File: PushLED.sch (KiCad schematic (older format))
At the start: 3 parts, among them Q1 BC847, SW3 SW_Push_LED

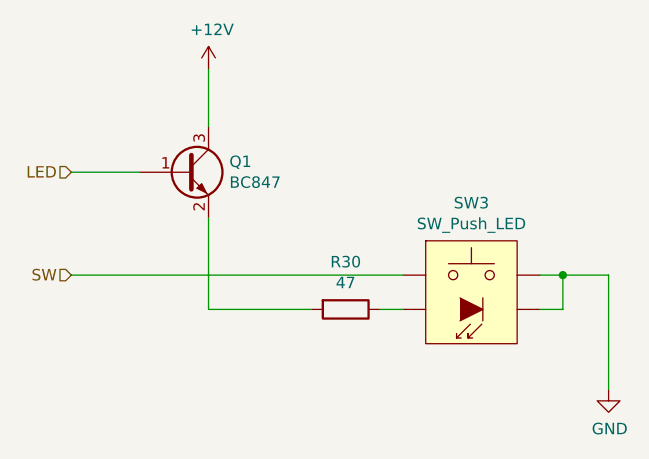
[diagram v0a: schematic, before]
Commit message: Moved codec to audio module.
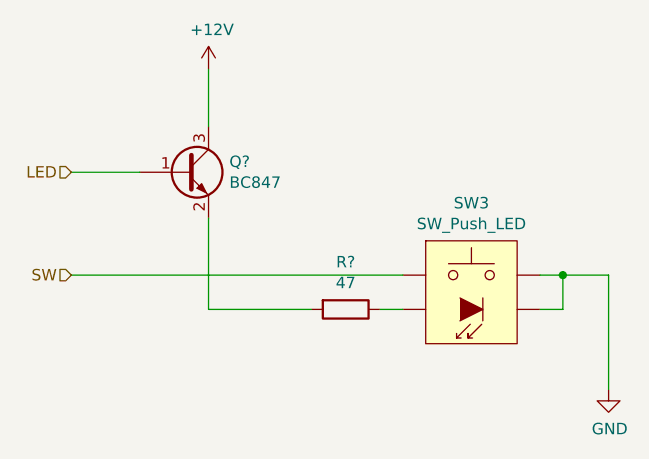
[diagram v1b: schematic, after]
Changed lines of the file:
@@
 AR Path="/61DB1EC2/5DB13571/5DA98203" Ref="#PWR?"  Part="1"
 AR Path="/61DC9CE4/5DA98203" Ref="#PWR055"  Part="1"
-F 0 "#PWR055" H 6250 4000 50  0001 C CNN
+AR Path="/6220B257/5DA98203" Ref="#PWR?"  Part="1"
+AR Path="/62210337/5DA98203" Ref="#PWR?"  Part="1"
+AR Path="/62210785/5DA98203" Ref="#PWR?"  Part="1"
+F 0 "#PWR?" H 6250 4000 50  0001 C CNN
 F 1 "GND" H 6255 4077 50  0000 C CNN
 F 2 "" H 6250 4250 50  0001 C CNN
@@
 AR Path="/61DB1EC2/5DB13571/5DA98210" Ref="R?"  Part="1"
 AR Path="/61DC9CE4/5DA98210" Ref="R30"  Part="1"
-F 0 "R30" V 4893 3900 50  0000 C CNN
+AR Path="/6220B257/5DA98210" Ref="R?"  Part="1"
+AR Path="/62210337/5DA98210" Ref="R?"  Part="1"
+AR Path="/62210785/5DA98210" Ref="R?"  Part="1"
+F 0 "R?" V 4893 3900 50  0000 C CNN
 F 1 "47" V 4984 3900 50  0000 C CNN
 F 2 "Resistor_SMD:R_0603_1608Metric" V 5030 3900 50  0001 C CNN
@@
 AR Path="/61DB1EC2/5DB13571/5DA9821D" Ref="Q?"  Part="1"
 AR Path="/61DC9CE4/5DA9821D" Ref="Q1"  Part="1"
-F 0 "Q1" H 4591 3346 50  0000 L CNN
+AR Path="/6220B257/5DA9821D" Ref="Q?"  Part="1"
+AR Path="/62210337/5DA9821D" Ref="Q?"  Part="1"
+AR Path="/62210785/5DA9821D" Ref="Q?"  Part="1"
+F 0 "Q?" H 4591 3346 50  0000 L CNN
 F 1 "BC847" H 4591 3255 50  0000 L CNN
 F 2 "Package_TO_SOT_SMD:SOT-23" H 4600 3225 50  0001 L CIN
@@
 AR Path="/61DB1EC2/5DB13571/5DA99988" Ref="#PWR?"  Part="1"
 AR Path="/61DC9CE4/5DA99988" Ref="#PWR054"  Part="1"
-F 0 "#PWR054" H 4500 2700 50  0001 C CNN
+AR Path="/6220B257/5DA99988" Ref="#PWR?"  Part="1"
+AR Path="/62210337/5DA99988" Ref="#PWR?"  Part="1"
+AR Path="/62210785/5DA99988" Ref="#PWR?"  Part="1"
+F 0 "#PWR?" H 4500 2700 50  0001 C CNN
 F 1 "+12V" H 4515 3023 50  0000 C CNN
 F 2 "" H 4500 2850 50  0001 C CNN
@@
 U 1 1 61E253E8
 P 5650 3750
-F 0 "SW3" H 5650 4065 50  0000 C CNN
+AR Path="/61DC9CE4/61E253E8" Ref="SW3"  Part="1"
+AR Path="/6220B257/61E253E8" Ref="SW?"  Part="1"
+AR Path="/62210337/61E253E8" Ref="SW?"  Part="1"
+AR Path="/62210785/61E253E8" Ref="SW?"  Part="1"
+F 0 "SW?" H 5650 4065 50  0000 C CNN
 F 1 "SW_Push_LED" H 5650 3974 50  0000 C CNN
 F 2 "" H 5650 3950 50  0001 C CNN

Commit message: Re-annotation.
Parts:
- added C26: 100n, symbol Device:C
- added R10: 10k, symbol Device:R
- renumbered R30 to R9
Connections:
- net GND: now also C26.2
- net SW: now also C26.1, R10.2
- new net +3V3: R10.1
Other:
- moved on the sheet: Q6
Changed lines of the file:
@@
 $Descr A4 11693 8268
 encoding utf-8
-Sheet 4 6
+Sheet 3 11
 Title ""
 Date ""
@@
 AR Path="/61DB1EC2/5E023019/5DA98203" Ref="#PWR?"  Part="1"
 AR Path="/61DB1EC2/5DB13571/5DA98203" Ref="#PWR?"  Part="1"
-AR Path="/61DC9CE4/5DA98203" Ref="#PWR055"  Part="1"
-AR Path="/6220B257/5DA98203" Ref="#PWR?"  Part="1"
-AR Path="/62210337/5DA98203" Ref="#PWR?"  Part="1"
-AR Path="/62210785/5DA98203" Ref="#PWR?"  Part="1"
-F 0 "#PWR?" H 6250 4000 50  0001 C CNN
+AR Path="/61DC9CE4/5DA98203" Ref="#PWR035"  Part="1"
+AR Path="/6220B257/5DA98203" Ref="#PWR092"  Part="1"
+AR Path="/62210337/5DA98203" Ref="#PWR096"  Part="1"
+AR Path="/62210785/5DA98203" Ref="#PWR0100"  Part="1"
+F 0 "#PWR0100" H 6250 4000 50  0001 C CNN
 F 1 "GND" H 6255 4077 50  0000 C CNN
 F 2 "" H 6250 4250 50  0001 C CNN
@@
 AR Path="/61DB1EC2/5E023019/5DA98210" Ref="R?"  Part="1"
 AR Path="/61DB1EC2/5DB13571/5DA98210" Ref="R?"  Part="1"
-AR Path="/61DC9CE4/5DA98210" Ref="R30"  Part="1"
-AR Path="/6220B257/5DA98210" Ref="R?"  Part="1"
-AR Path="/62210337/5DA98210" Ref="R?"  Part="1"
-AR Path="/62210785/5DA98210" Ref="R?"  Part="1"
-F 0 "R?" V 4893 3900 50  0000 C CNN
+AR Path="/61DC9CE4/5DA98210" Ref="R9"  Part="1"
+AR Path="/6220B257/5DA98210" Ref="R60"  Part="1"
+AR Path="/62210337/5DA98210" Ref="R62"  Part="1"
+AR Path="/62210785/5DA98210" Ref="R64"  Part="1"
+F 0 "R64" V 4893 3900 50  0000 C CNN
 F 1 "47" V 4984 3900 50  0000 C CNN
 F 2 "Resistor_SMD:R_0603_1608Metric" V 5030 3900 50  0001 C CNN
@@
 L Transistor_BJT:BC847 Q?
 U 1 1 5DA9821D
-P 4400 3300
+P 4550 3300
 AR Path="/5C756F9B/5DA9821D" Ref="Q?"  Part="1"
 AR Path="/5C763CB7/5DA9821D" Ref="Q?"  Part="1"
@@
 AR Path="/61DB1EC2/5DB13571/5DA9821D" Ref="Q?"  Part="1"
 AR Path="/61DC9CE4/5DA9821D" Ref="Q1"  Part="1"
-AR Path="/6220B257/5DA9821D" Ref="Q?"  Part="1"
-AR Path="/62210337/5DA9821D" Ref="Q?"  Part="1"
-AR Path="/62210785/5DA9821D" Ref="Q?"  Part="1"
-F 0 "Q?" H 4591 3346 50  0000 L CNN
-F 1 "BC847" H 4591 3255 50  0000 L CNN
-F 2 "Package_TO_SOT_SMD:SOT-23" H 4600 3225 50  0001 L CIN
-F 3 "http://www.infineon.com/dgdl/Infineon-BC847SERIES_BC848SERIES_BC849SERIES_BC850SERIES-DS-v01_01-en.pdf?fileId=db3a304314dca389011541d4630a1657" H 4400 3300 50  0001 L CNN
-	1    4400 3300
-	1    0    0    -1
-$EndComp
-Wire Wire Line
-	4500 3500 4500 3900
-Wire Wire Line
-	4500 3900 4950 3900
+AR Path="/6220B257/5DA9821D" Ref="Q4"  Part="1"
+AR Path="/62210337/5DA9821D" Ref="Q5"  Part="1"
+AR Path="/62210785/5DA9821D" Ref="Q6"  Part="1"
+F 0 "Q6" H 4741 3346 50  0000 L CNN
+F 1 "BC847" H 4741 3255 50  0000 L CNN
+F 2 "Package_TO_SOT_SMD:SOT-23" H 4750 3225 50  0001 L CIN
+F 3 "http://www.infineon.com/dgdl/Infineon-BC847SERIES_BC848SERIES_BC849SERIES_BC850SERIES-DS-v01_01-en.pdf?fileId=db3a304314dca389011541d4630a1657" H 4550 3300 50  0001 L CNN
+	1    4550 3300
+	1    0    0    -1
+$EndComp
+Wire Wire Line
+	4650 3500 4650 3900
 Text HLabel 3900 3300 0    50   Input ~ 0
 LED
-Wire Wire Line
-	3900 3300 4200 3300
 Text HLabel 3900 3750 0    50   Input ~ 0
 SW
-Wire Wire Line
-	3900 3750 5350 3750
 $Comp
 L power:+12V #PWR?
 U 1 1 5DA99988
-P 4500 2850
+P 4650 2850
 AR Path="/5DA90748/5DA99988" Ref="#PWR?"  Part="1"
 AR Path="/5DAF110B/5DA99988" Ref="#PWR?"  Part="1"
@@
 AR Path="/61DB1EC2/5E023019/5DA99988" Ref="#PWR?"  Part="1"
 AR Path="/61DB1EC2/5DB13571/5DA99988" Ref="#PWR?"  Part="1"
-AR Path="/61DC9CE4/5DA99988" Ref="#PWR054"  Part="1"
-AR Path="/6220B257/5DA99988" Ref="#PWR?"  Part="1"
-AR Path="/62210337/5DA99988" Ref="#PWR?"  Part="1"
-AR Path="/62210785/5DA99988" Ref="#PWR?"  Part="1"
-F 0 "#PWR?" H 4500 2700 50  0001 C CNN
-F 1 "+12V" H 4515 3023 50  0000 C CNN
-F 2 "" H 4500 2850 50  0001 C CNN
-F 3 "" H 4500 2850 50  0001 C CNN
-	1    4500 2850
-	1    0    0    -1
-$EndComp
-Wire Wire Line
-	4500 2850 4500 3100
+AR Path="/61DC9CE4/5DA99988" Ref="#PWR033"  Part="1"
+AR Path="/6220B257/5DA99988" Ref="#PWR090"  Part="1"
+AR Path="/62210337/5DA99988" Ref="#PWR094"  Part="1"
+AR Path="/62210785/5DA99988" Ref="#PWR098"  Part="1"
+F 0 "#PWR098" H 4650 2700 50  0001 C CNN
+F 1 "+12V" H 4665 3023 50  0000 C CNN
+F 2 "" H 4650 2850 50  0001 C CNN
+F 3 "" H 4650 2850 50  0001 C CNN
+	1    4650 2850
+	1    0    0    -1
+$EndComp
+Wire Wire Line
+	4650 2850 4650 3100
 $Comp
 L SW_PUSH_LED:SW_Push_LED SW3
@@
 P 5650 3750
 AR Path="/61DC9CE4/61E253E8" Ref="SW3"  Part="1"
-AR Path="/6220B257/61E253E8" Ref="SW?"  Part="1"
-AR Path="/62210337/61E253E8" Ref="SW?"  Part="1"
-AR Path="/62210785/61E253E8" Ref="SW?"  Part="1"
-F 0 "SW?" H 5650 4065 50  0000 C CNN
+AR Path="/6220B257/61E253E8" Ref="SW4"  Part="1"
+AR Path="/62210337/61E253E8" Ref="SW5"  Part="1"
+AR Path="/62210785/61E253E8" Ref="SW6"  Part="1"
+F 0 "SW6" H 5650 4065 50  0000 C CNN
 F 1 "SW_Push_LED" H 5650 3974 50  0000 C CNN
 F 2 "" H 5650 3950 50  0001 C CNN
@@
 	1    0    0    -1
 $EndComp
+$Comp
+L Device:C C26
+U 1 1 62217CA5
+P 4200 4000
+AR Path="/61DC9CE4/62217CA5" Ref="C26"  Part="1"
+AR Path="/6220B257/62217CA5" Ref="C55"  Part="1"
+AR Path="/62210337/62217CA5" Ref="C56"  Part="1"
+AR Path="/62210785/62217CA5" Ref="C57"  Part="1"
+F 0 "C57" H 4315 4046 50  0000 L CNN
+F 1 "100n" H 4315 3955 50  0000 L CNN
+F 2 "" H 4238 3850 50  0001 C CNN
+F 3 "~" H 4200 4000 50  0001 C CNN
+	1    4200 4000
+	1    0    0    -1
+$EndComp
+$Comp
+L power:GND #PWR?
+U 1 1 622189BA
+P 4200 4250
+AR Path="/622189BA" Ref="#PWR?"  Part="1"
+AR Path="/5DA90748/622189BA" Ref="#PWR?"  Part="1"
+AR Path="/5DAF110B/622189BA" Ref="#PWR?"  Part="1"
+AR Path="/5DB16B82/622189BA" Ref="#PWR?"  Part="1"
+AR Path="/5DB16B86/622189BA" Ref="#PWR?"  Part="1"
+AR Path="/5DB3CAB0/622189BA" Ref="#PWR?"  Part="1"
+AR Path="/5DB3CAB4/622189BA" Ref="#PWR?"  Part="1"
+AR Path="/5DB3CAB8/622189BA" Ref="#PWR?"  Part="1"
+AR Path="/5DB3CABC/622189BA" Ref="#PWR?"  Part="1"
+AR Path="/5DB87BB5/622189BA" Ref="#PWR?"  Part="1"
+AR Path="/5DB87BB9/622189BA" Ref="#PWR?"  Part="1"
+AR Path="/5DB87BBD/622189BA" Ref="#PWR?"  Part="1"
+AR Path="/5DD41DD6/5DA90748/622189BA" Ref="#PWR?"  Part="1"
+AR Path="/5DD41DD6/5DAF110B/622189BA" Ref="#PWR?"  Part="1"
+AR Path="/5DD41DD6/5DB16B82/622189BA" Ref="#PWR?"  Part="1"
+AR Path="/5DD41DD6/5DB16B86/622189BA" Ref="#PWR?"  Part="1"
+AR Path="/5DD41DD6/5DB3CAB0/622189BA" Ref="#PWR?"  Part="1"
+AR Path="/5DD41DD6/5DB3CAB4/622189BA" Ref="#PWR?"  Part="1"
+AR Path="/5DD41DD6/5DB3CAB8/622189BA" Ref="#PWR?"  Part="1"
+AR Path="/5DD41DD6/5DB3CABC/622189BA" Ref="#PWR?"  Part="1"
+AR Path="/5DD41DD6/5DB87BB5/622189BA" Ref="#PWR?"  Part="1"
+AR Path="/5DD41DD6/5DB87BB9/622189BA" Ref="#PWR?"  Part="1"
+AR Path="/5DD41DD6/5DB87BBD/622189BA" Ref="#PWR?"  Part="1"
+AR Path="/5DE2B991/622189BA" Ref="#PWR?"  Part="1"
+AR Path="/5E016F8F/622189BA" Ref="#PWR?"  Part="1"
+AR Path="/5E023019/622189BA" Ref="#PWR?"  Part="1"
+AR Path="/5DB13571/622189BA" Ref="#PWR?"  Part="1"
+AR Path="/5FF0E759/5DE2B991/622189BA" Ref="#PWR?"  Part="1"
+AR Path="/5FF0E759/5E016F8F/622189BA" Ref="#PWR?"  Part="1"
+AR Path="/5FF0E759/5E023019/622189BA" Ref="#PWR?"  Part="1"
+AR Path="/5FF0E759/5DB13571/622189BA" Ref="#PWR?"  Part="1"
+AR Path="/600106C3/622189BA" Ref="#PWR?"  Part="1"
+AR Path="/60010733/622189BA" Ref="#PWR?"  Part="1"
+AR Path="/6001073B/622189BA" Ref="#PWR?"  Part="1"
+AR Path="/60010823/622189BA" Ref="#PWR?"  Part="1"
+AR Path="/61DB1EC2/5DE2B991/622189BA" Ref="#PWR?"  Part="1"
+AR Path="/61DB1EC2/5E016F8F/622189BA" Ref="#PWR?"  Part="1"
+AR Path="/61DB1EC2/5E023019/622189BA" Ref="#PWR?"  Part="1"
+AR Path="/61DB1EC2/5DB13571/622189BA" Ref="#PWR?"  Part="1"
+AR Path="/61DC9CE4/622189BA" Ref="#PWR032"  Part="1"
+AR Path="/6220B257/622189BA" Ref="#PWR089"  Part="1"
+AR Path="/62210337/622189BA" Ref="#PWR093"  Part="1"
+AR Path="/62210785/622189BA" Ref="#PWR097"  Part="1"
+F 0 "#PWR097" H 4200 4000 50  0001 C CNN
+F 1 "GND" H 4205 4077 50  0000 C CNN
+F 2 "" H 4200 4250 50  0001 C CNN
+F 3 "" H 4200 4250 50  0001 C CNN
+	1    4200 4250
+	1    0    0    -1
+$EndComp
+Wire Wire Line
+	4200 4250 4200 4150
+Wire Wire Line
+	4200 3850 4200 3750
+Wire Wire Line
+	3900 3750 4200 3750
+Connection ~ 4200 3750
+Wire Wire Line
+	4200 3750 5250 3750
+$Comp
+L Device:R R10
+U 1 1 622197B8
+P 5250 3300
+AR Path="/61DC9CE4/622197B8" Ref="R10"  Part="1"
+AR Path="/6220B257/622197B8" Ref="R61"  Part="1"
+AR Path="/62210337/622197B8" Ref="R63"  Part="1"
+AR Path="/62210785/622197B8" Ref="R65"  Part="1"
+F 0 "R65" H 5320 3346 50  0000 L CNN
+F 1 "10k" H 5320 3255 50  0000 L CNN
+F 2 "" V 5180 3300 50  0001 C CNN
+F 3 "~" H 5250 3300 50  0001 C CNN
+	1    5250 3300
+	1    0    0    -1
+$EndComp
+Wire Wire Line
+	4650 3900 4950 3900
+Wire Wire Line
+	3900 3300 4350 3300
+Wire Wire Line
+	5250 3450 5250 3750
+Connection ~ 5250 3750
+Wire Wire Line
+	5250 3750 5350 3750
+$Comp
+L power:+3.3V #PWR034
+U 1 1 6221CF68
+P 5250 2850
+AR Path="/61DC9CE4/6221CF68" Ref="#PWR034"  Part="1"
+AR Path="/6220B257/6221CF68" Ref="#PWR091"  Part="1"
+AR Path="/62210337/6221CF68" Ref="#PWR095"  Part="1"
+AR Path="/62210785/6221CF68" Ref="#PWR099"  Part="1"
+F 0 "#PWR099" H 5250 2700 50  0001 C CNN
+F 1 "+3.3V" H 5265 3023 50  0000 C CNN
+F 2 "" H 5250 2850 50  0001 C CNN
+F 3 "" H 5250 2850 50  0001 C CNN
+	1    5250 2850
+	1    0    0    -1
+$EndComp
+Wire Wire Line
+	5250 2850 5250 3150
 $EndSCHEMATC

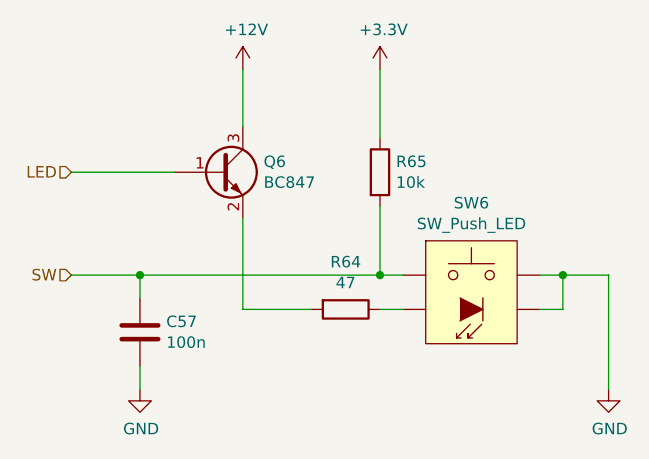
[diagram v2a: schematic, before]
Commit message: Assigned pins and cleared schema rules.
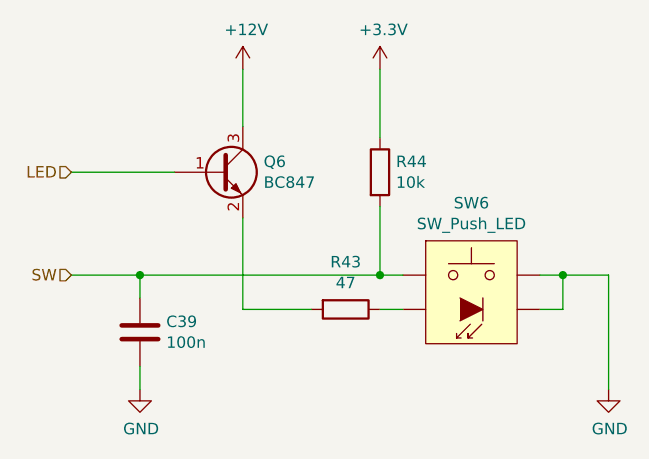
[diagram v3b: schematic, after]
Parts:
- C26: footprint (none) -> Capacitor_SMD:C_0402_1005Metric
- R10: footprint (none) -> Resistor_SMD:R_0603_1608Metric
- SW3: footprint (none) -> Local:SW_PUSH_LED_6mm
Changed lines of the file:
@@
 $Descr A4 11693 8268
 encoding utf-8
-Sheet 3 11
+Sheet 10 11
 Title ""
 Date ""
@@
 AR Path="/61DB1EC2/5E023019/5DA98203" Ref="#PWR?"  Part="1"
 AR Path="/61DB1EC2/5DB13571/5DA98203" Ref="#PWR?"  Part="1"
-AR Path="/61DC9CE4/5DA98203" Ref="#PWR035"  Part="1"
-AR Path="/6220B257/5DA98203" Ref="#PWR092"  Part="1"
-AR Path="/62210337/5DA98203" Ref="#PWR096"  Part="1"
-AR Path="/62210785/5DA98203" Ref="#PWR0100"  Part="1"
-F 0 "#PWR0100" H 6250 4000 50  0001 C CNN
+AR Path="/61DC9CE4/5DA98203" Ref="#PWR037"  Part="1"
+AR Path="/6220B257/5DA98203" Ref="#PWR067"  Part="1"
+AR Path="/62210337/5DA98203" Ref="#PWR071"  Part="1"
+AR Path="/62210785/5DA98203" Ref="#PWR075"  Part="1"
+F 0 "#PWR075" H 6250 4000 50  0001 C CNN
 F 1 "GND" H 6255 4077 50  0000 C CNN
 F 2 "" H 6250 4250 50  0001 C CNN
@@
 AR Path="/61DB1EC2/5DB13571/5DA98210" Ref="R?"  Part="1"
 AR Path="/61DC9CE4/5DA98210" Ref="R9"  Part="1"
-AR Path="/6220B257/5DA98210" Ref="R60"  Part="1"
-AR Path="/62210337/5DA98210" Ref="R62"  Part="1"
-AR Path="/62210785/5DA98210" Ref="R64"  Part="1"
-F 0 "R64" V 4893 3900 50  0000 C CNN
+AR Path="/6220B257/5DA98210" Ref="R39"  Part="1"
+AR Path="/62210337/5DA98210" Ref="R41"  Part="1"
+AR Path="/62210785/5DA98210" Ref="R43"  Part="1"
+F 0 "R43" V 4893 3900 50  0000 C CNN
 F 1 "47" V 4984 3900 50  0000 C CNN
 F 2 "Resistor_SMD:R_0603_1608Metric" V 5030 3900 50  0001 C CNN
@@
 AR Path="/61DB1EC2/5E023019/5DA99988" Ref="#PWR?"  Part="1"
 AR Path="/61DB1EC2/5DB13571/5DA99988" Ref="#PWR?"  Part="1"
-AR Path="/61DC9CE4/5DA99988" Ref="#PWR033"  Part="1"
-AR Path="/6220B257/5DA99988" Ref="#PWR090"  Part="1"
-AR Path="/62210337/5DA99988" Ref="#PWR094"  Part="1"
-AR Path="/62210785/5DA99988" Ref="#PWR098"  Part="1"
-F 0 "#PWR098" H 4650 2700 50  0001 C CNN
+AR Path="/61DC9CE4/5DA99988" Ref="#PWR035"  Part="1"
+AR Path="/6220B257/5DA99988" Ref="#PWR065"  Part="1"
+AR Path="/62210337/5DA99988" Ref="#PWR069"  Part="1"
+AR Path="/62210785/5DA99988" Ref="#PWR073"  Part="1"
+F 0 "#PWR073" H 4650 2700 50  0001 C CNN
 F 1 "+12V" H 4665 3023 50  0000 C CNN
 F 2 "" H 4650 2850 50  0001 C CNN
@@
 F 0 "SW6" H 5650 4065 50  0000 C CNN
 F 1 "SW_Push_LED" H 5650 3974 50  0000 C CNN
-F 2 "" H 5650 3950 50  0001 C CNN
+F 2 "Local:SW_PUSH_LED_6mm" H 5650 3950 50  0001 C CNN
 F 3 "" H 5650 3950 50  0001 C CNN
 	1    5650 3750
@@
 P 4200 4000
 AR Path="/61DC9CE4/62217CA5" Ref="C26"  Part="1"
-AR Path="/6220B257/62217CA5" Ref="C55"  Part="1"
-AR Path="/62210337/62217CA5" Ref="C56"  Part="1"
-AR Path="/62210785/62217CA5" Ref="C57"  Part="1"
-F 0 "C57" H 4315 4046 50  0000 L CNN
+AR Path="/6220B257/62217CA5" Ref="C37"  Part="1"
+AR Path="/62210337/62217CA5" Ref="C38"  Part="1"
+AR Path="/62210785/62217CA5" Ref="C39"  Part="1"
+F 0 "C39" H 4315 4046 50  0000 L CNN
 F 1 "100n" H 4315 3955 50  0000 L CNN
-F 2 "" H 4238 3850 50  0001 C CNN
+F 2 "Capacitor_SMD:C_0402_1005Metric" H 4238 3850 50  0001 C CNN
 F 3 "~" H 4200 4000 50  0001 C CNN
 	1    4200 4000
@@
 AR Path="/61DB1EC2/5E023019/622189BA" Ref="#PWR?"  Part="1"
 AR Path="/61DB1EC2/5DB13571/622189BA" Ref="#PWR?"  Part="1"
-AR Path="/61DC9CE4/622189BA" Ref="#PWR032"  Part="1"
-AR Path="/6220B257/622189BA" Ref="#PWR089"  Part="1"
-AR Path="/62210337/622189BA" Ref="#PWR093"  Part="1"
-AR Path="/62210785/622189BA" Ref="#PWR097"  Part="1"
-F 0 "#PWR097" H 4200 4000 50  0001 C CNN
+AR Path="/61DC9CE4/622189BA" Ref="#PWR034"  Part="1"
+AR Path="/6220B257/622189BA" Ref="#PWR064"  Part="1"
+AR Path="/62210337/622189BA" Ref="#PWR068"  Part="1"
+AR Path="/62210785/622189BA" Ref="#PWR072"  Part="1"
+F 0 "#PWR072" H 4200 4000 50  0001 C CNN
 F 1 "GND" H 4205 4077 50  0000 C CNN
 F 2 "" H 4200 4250 50  0001 C CNN
@@
 P 5250 3300
 AR Path="/61DC9CE4/622197B8" Ref="R10"  Part="1"
-AR Path="/6220B257/622197B8" Ref="R61"  Part="1"
-AR Path="/62210337/622197B8" Ref="R63"  Part="1"
-AR Path="/62210785/622197B8" Ref="R65"  Part="1"
-F 0 "R65" H 5320 3346 50  0000 L CNN
+AR Path="/6220B257/622197B8" Ref="R40"  Part="1"
+AR Path="/62210337/622197B8" Ref="R42"  Part="1"
+AR Path="/62210785/622197B8" Ref="R44"  Part="1"
+F 0 "R44" H 5320 3346 50  0000 L CNN
 F 1 "10k" H 5320 3255 50  0000 L CNN
-F 2 "" V 5180 3300 50  0001 C CNN
+F 2 "Resistor_SMD:R_0603_1608Metric" V 5180 3300 50  0001 C CNN
 F 3 "~" H 5250 3300 50  0001 C CNN
 	1    5250 3300
@@
 	5250 3750 5350 3750
 $Comp
-L power:+3.3V #PWR034
+L power:+3.3V #PWR036
 U 1 1 6221CF68
 P 5250 2850
-AR Path="/61DC9CE4/6221CF68" Ref="#PWR034"  Part="1"
-AR Path="/6220B257/6221CF68" Ref="#PWR091"  Part="1"
-AR Path="/62210337/6221CF68" Ref="#PWR095"  Part="1"
-AR Path="/62210785/6221CF68" Ref="#PWR099"  Part="1"
-F 0 "#PWR099" H 5250 2700 50  0001 C CNN
+AR Path="/61DC9CE4/6221CF68" Ref="#PWR036"  Part="1"
+AR Path="/6220B257/6221CF68" Ref="#PWR066"  Part="1"
+AR Path="/62210337/6221CF68" Ref="#PWR070"  Part="1"
+AR Path="/62210785/6221CF68" Ref="#PWR074"  Part="1"
+F 0 "#PWR074" H 5250 2700 50  0001 C CNN
 F 1 "+3.3V" H 5265 3023 50  0000 C CNN
 F 2 "" H 5250 2850 50  0001 C CNN
